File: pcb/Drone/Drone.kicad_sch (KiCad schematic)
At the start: 64 parts, among them J1 USB_C_Receptacle_USB2.0_16P, J10 JST1.25, J2 JST1.25, J3 JST1.25, J4 JST1.25, J5 JST1.25, J6 JST1.25, J7 JST1.25, J8 JST1.25, J9 JST1.25, Q1 SS8050, Q2 SS8050, Q3 Si2301, SW1 RST, SW2 BOOT, U1 esp32s3_wroom1, U2 DW01A, U3 AP2112K-3.3, U3 GY-87, U4 USBLC6-2SC6, U5 8205, U6 CP2102, U9 ME6211C33M5

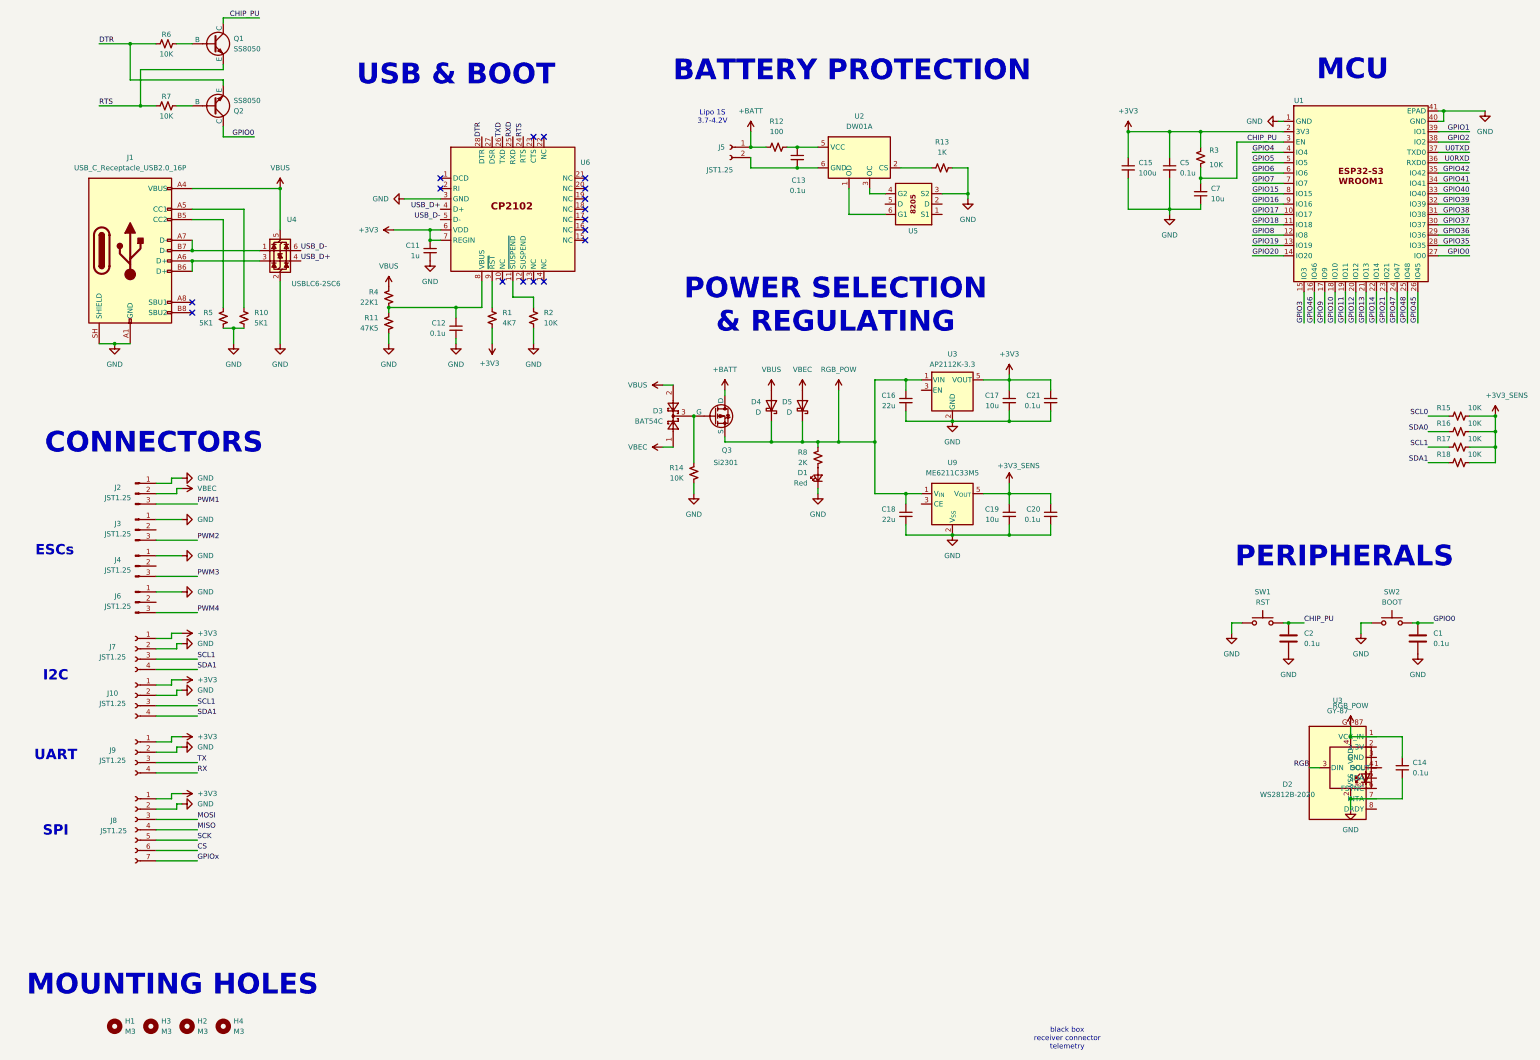
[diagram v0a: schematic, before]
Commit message: added gy87
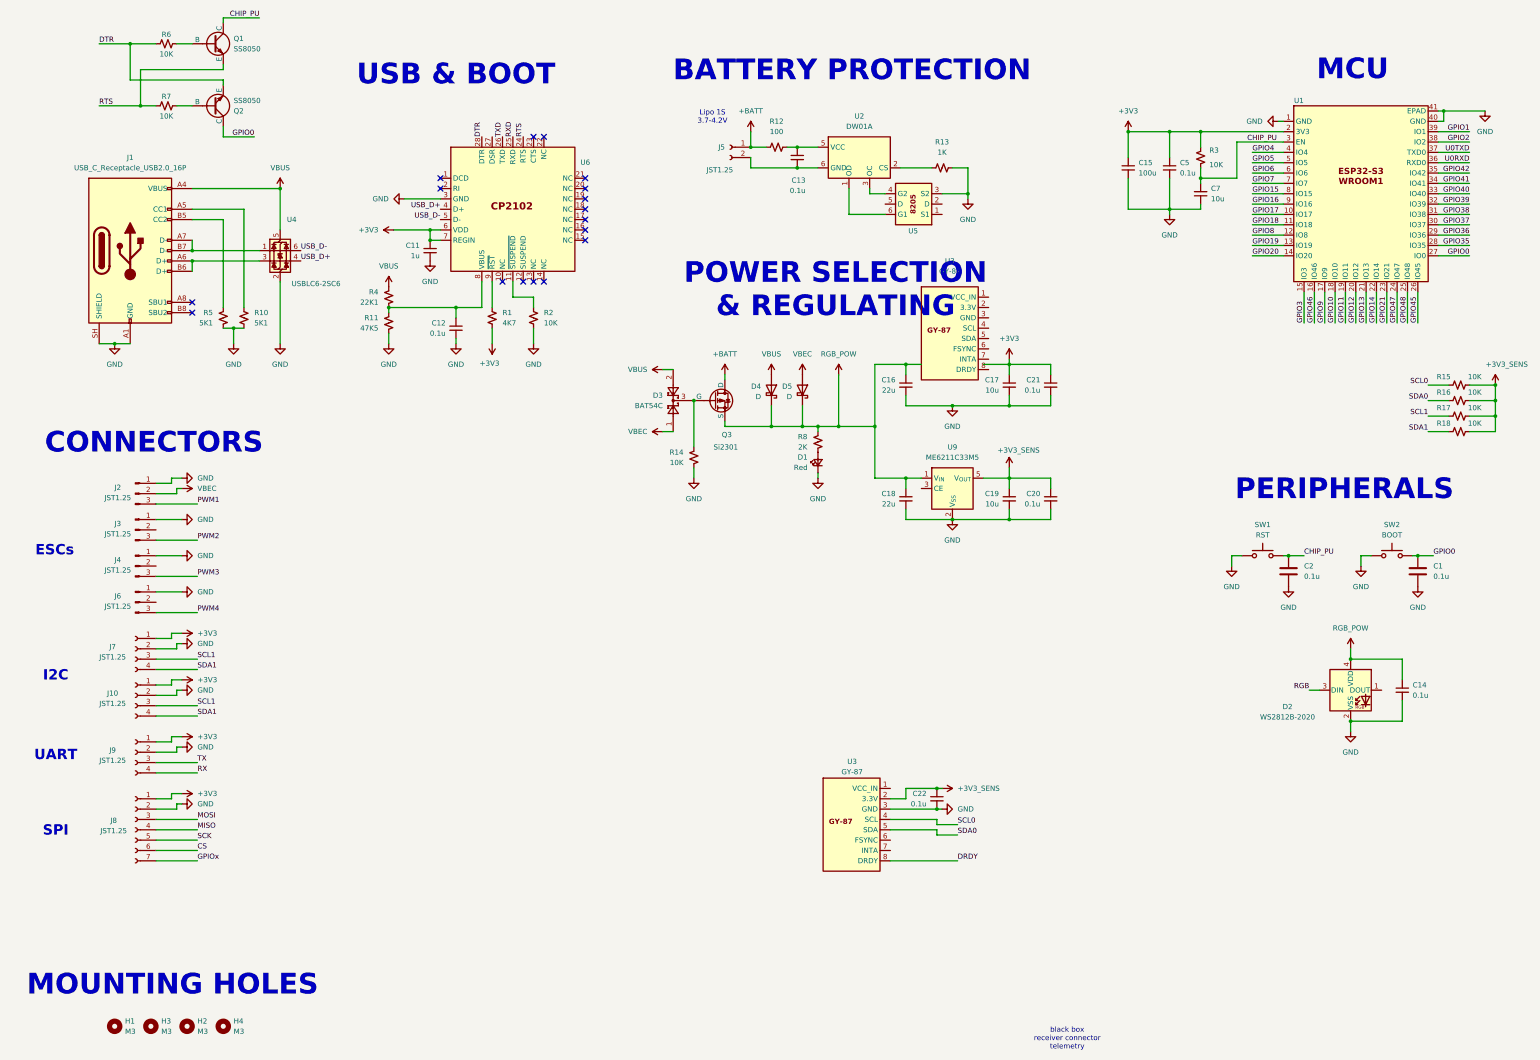
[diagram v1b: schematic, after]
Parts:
- added C22: 0.1u, Capacitor_SMD:C_0805_2012Metric, symbol Device:C_Small
- U3: value AP2112K-3.3 -> GY-87; footprint Package_TO_SOT_SMD:SOT-23-5 -> GY-87:GY-87
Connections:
- net +3V3: no longer U3.5 (VOUT)
- net +3V3_SENS: now also U3.2 (3.3V), C22.1
- net GND: now also U3.3 (GND), C22.2; no longer U3.2 (GND)
- net RGB_POW: no longer U3.1 (VIN)
- net SCL0: now also U3.4 (SCL)
- net SDA0: now also U3.5 (SDA)
- net DRDY: now reaches U3.8 (DRDY)
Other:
- moved on the sheet: C1, C14, C16, C17, C18, C19, C2, C20, C21, D1, D2, D3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

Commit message: hello
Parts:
- removed U3: GY-87, GY-87:GY-87, symbol Regulator_Linear:AP2112K-3.3
- added U7: AP2112K-3.3, Package_TO_SOT_SMD:SOT-23-5, symbol Regulator_Linear:AP2112K-3.3
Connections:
- net +3V3: now also U7.5 (VOUT)
- net GND: now also U7.2 (GND)
- net RGB_POW: now also U7.1 (VIN)
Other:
- note added: "10DOF IMU"
- moved on the sheet: C22, U3
